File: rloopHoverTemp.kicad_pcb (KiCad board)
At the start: 2 copper layers, 30.5 x 39.4 mm, 28 parts, among them P1 CONN_01X02, P2 CONN_01X02, P3 CONN_01X01, P4 CONN_01X01, Q1 Q_NPN_BEC, Q2 Q_NPN_BEC, U1 XTR117, U2 TS305-10C50, U3 LTC2054, U4 XTR117, U5 LTC2054

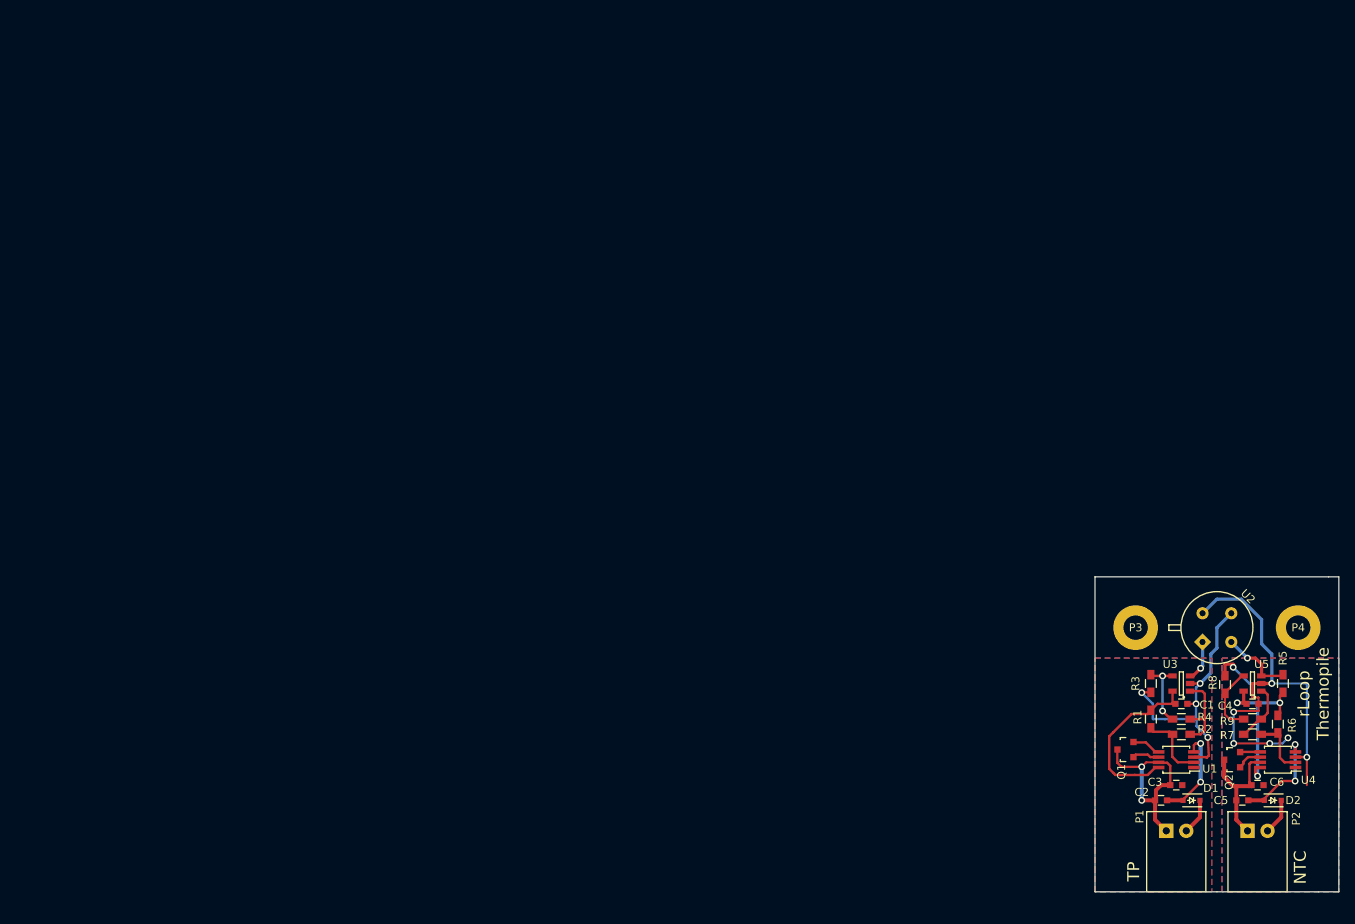
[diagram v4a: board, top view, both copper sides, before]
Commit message: complete redo with MLX sensor
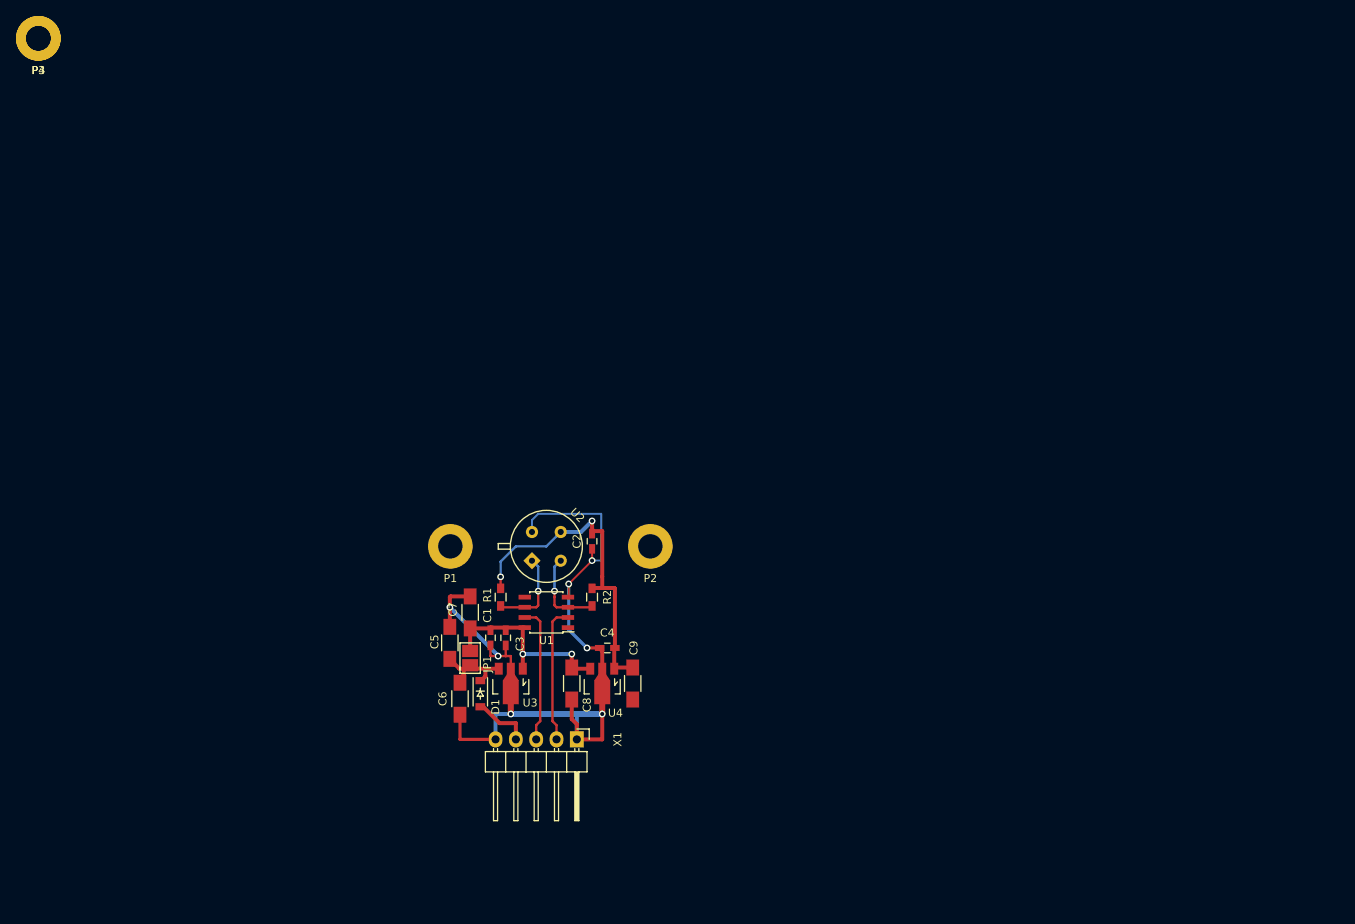
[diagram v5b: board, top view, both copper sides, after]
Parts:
- removed D2: D_Small, -footprints:SOD-323
- removed Q1, Q2: Q_NPN_BEC, TO_SOT_Packages_SMD:SOT-23
- removed R3: 825, Resistors_SMD:R_0603_HandSoldering
- removed R4: 470K, Resistors_SMD:R_0603_HandSoldering
- removed R5, R8: 100K, Resistors_SMD:R_0603_HandSoldering
- removed R6: 125K, Resistors_SMD:R_0603_HandSoldering
- removed R7: 25K, Resistors_SMD:R_0603_HandSoldering
- removed R9: 10K, Resistors_SMD:R_0603_HandSoldering
- removed U5: LTC2054, TO_SOT_Packages_SMD:SOT-23-5
- added C7: 4u7, Capacitors_SMD:C_1206_HandSoldering, F.Cu at (54.0, 71.8)
- added C8: 4u7, Capacitors_SMD:C_1206_HandSoldering, F.Cu at (66.7, 80.6)
- added C9: 4u7, Capacitors_SMD:C_1206_HandSoldering, F.Cu at (74.3, 80.6)
- added JP1: Jumper_NC_Small, -footprints:SOLDERJUMPER, F.Cu at (54.0, 77.5)
- added X1: CONN_01X05, Pin_Headers:Pin_Header_Angled_1x05, F.Cu at (67.3, 87.6)
- C1: value 100n -> C; footprint Capacitors_SMD:C_0603 -> Capacitors_SMD:C_0603_HandSoldering
- C2, C4: footprint Capacitors_SMD:C_0603 -> Capacitors_SMD:C_0603_HandSoldering
- C3: value 10n -> C; footprint Capacitors_SMD:C_0603 -> Capacitors_SMD:C_0603_HandSoldering
- C5: value 100n -> 4u7; footprint Capacitors_SMD:C_0603 -> Capacitors_SMD:C_1206_HandSoldering
- C6: value 10n -> 4u7; footprint Capacitors_SMD:C_0603 -> Capacitors_SMD:C_1206_HandSoldering
- D1: value D_Small -> D; footprint -footprints:SOD-323 -> Diodes_SMD:SOD-123
- P1, P2: value CONN_01X02 -> CONN_01X01; footprint -footprints:CONN-JST-XH-2-PTH-RGT -> -footprints:SCREWPAD-4-40
- R1: value 125K -> 4K7
- R2: value 25K -> 4K7
- U1: value XTR117 -> P82B715TD; footprint Housings_SSOP:MSOP-8_3x3mm_Pitch0.65mm -> Housings_SOIC:SOIC-8_3.9x4.9mm_Pitch1.27mm
- U2: value TS305-10C50 -> MLX90614; footprint -footprints:TS305-10C50 -> -footprints:TO39
- U3: value LTC2054 -> Regulator; footprint TO_SOT_Packages_SMD:SOT-23-5 -> -footprints:SOT89-3-VREG
- U4: value XTR117 -> Regulator; footprint Housings_SSOP:MSOP-8_3x3mm_Pitch0.65mm -> -footprints:SOT89-3-VREG
- moved P4 173.9 mm to (0.00, 0.00)
- moved P3 155.7 mm to (0.00, 0.00)
- moved C5 102.5 mm to (51.4, 75.6), turned to 90 degrees
- moved C6 98.6 mm to (52.7, 82.5), turned to 270 degrees
- moved P1 97.5 mm to (51.5, 63.5), turned to 0 degrees
- moved D1 89.9 mm to (55.2, 81.9), turned to 270 degrees
- moved C3 86.2 mm to (56.5, 74.9), turned to 270 degrees
- moved U4 85.0 mm to (70.5, 80.6)
- moved C1 84.9 mm to (58.4, 74.9), turned to 90 degrees
- moved U2 84.4 mm to (63.5, 63.5)
- moved U3 83.8 mm to (59.1, 80.6)
- moved P2 83.8 mm to (76.5, 63.5), turned to 0 degrees
- moved R1 82.7 mm to (57.8, 69.8)
- moved C4 80.9 mm to (71.1, 76.2), turned to 0 degrees
- moved U1 80.9 mm to (63.5, 71.8)
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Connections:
- C1 pad 1: /GNDA -> GND
- C1 pad 2: Net-(C1-Pad2) -> +12V
- C2 pad 1: /GNDA -> GND
- C2 pad 2: /24V_A -> +5V
- C3 pad 1: /24V_A -> +12V
- C3 pad 2: Net-(C3-Pad2) -> GND
- C4 pad 1: /GNDB -> GND
- C4 pad 2: Net-(C4-Pad2) -> +5V
- C5 pad 1: /GNDB -> Net-(C5-Pad1)
- C5 pad 2: /24V_B -> GND
- C6 pad 1: /24V_B -> Net-(C5-Pad1)
- C6 pad 2: Net-(C6-Pad2) -> GND
- D1 pad 1: Net-(D1-Pad1) -> Net-(C5-Pad1)
- D1 pad 2: Net-(C3-Pad2) -> +24V
- P1 pad 1: /24V_A -> Net-(P1-Pad1)
- P2 pad 1: /24V_B -> Net-(P2-Pad1)
- R1 pad 1: Net-(C1-Pad2) -> +5V
- R2 pad 1: Net-(R1-Pad2) -> +5V
- U1 pad 2: Net-(R1-Pad2) -> SDA
- U1 pad 3: /GNDA -> Net-(R2-Pad2)
- U1 pad 4: Net-(C3-Pad2) -> GND
- U1 pad 6: Net-(Q1-Pad1) -> Net-(R1-Pad2)
- U1 pad 7: /24V_A -> SCL
- U1 pad 8: Net-(C1-Pad2) -> +12V
- U2 pad 1: Net-(U2-Pad1) -> Net-(R1-Pad2)
- U2 pad 2: Net-(R5-Pad2) -> Net-(R2-Pad2)
- U2 pad 3: /GNDA -> +5V
- U2 pad 4: /GNDB -> GND
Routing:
- net GND: track 0.00 -> 104.3 mm, vias 0 -> 7
- net /GNDB: track 65.7 -> 0.00 mm, vias 7 -> 0
- net +5V: track 0.00 -> 42.8 mm, vias 0 -> 2
- net /GNDA: track 35.1 -> 0.00 mm, vias 4 -> 0
- net +12V: track 0.00 -> 26.2 mm, vias 0 -> 2
- net /24V_A: track 25.1 -> 0.00 mm, vias 2 -> 0
- net Net-(C1-Pad2): track 22.8 -> 0.00 mm
- net Net-(C4-Pad2): track 22.7 -> 0.00 mm, vias 3 -> 0
- net SCL: track 0.00 -> 17.1 mm
- net SDA: track 0.00 -> 17.1 mm
- net /24V_B: track 16.9 -> 0.00 mm
- net Net-(C6-Pad2): track 12.5 -> 0.00 mm, vias 2 -> 0
- net Net-(C3-Pad2): track 12.1 -> 0.00 mm, vias 2 -> 0
- net Net-(C5-Pad1): track 0.00 -> 11.7 mm
- net Net-(R5-Pad2): track 9.37 -> 0.00 mm, vias 1 -> 0
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- removed copper zone on B.Cu, net /GNDA
- removed copper zone on F.Cu, net /GNDA
- removed copper zone on B.Cu, net /GNDB
- removed copper zone on F.Cu, net /GNDB
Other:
- board outline removed
- net class 24V removed
- net class Default: clearance 0.254 -> 0.25; trace_width 0.254 -> 0.25
- rule trace_clearance: 0.254 -> 0.25
- board text removed: "NTC"
- board text removed: "TP"
- board text removed: "rLoop Thermopile"

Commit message: dual MNL connector version
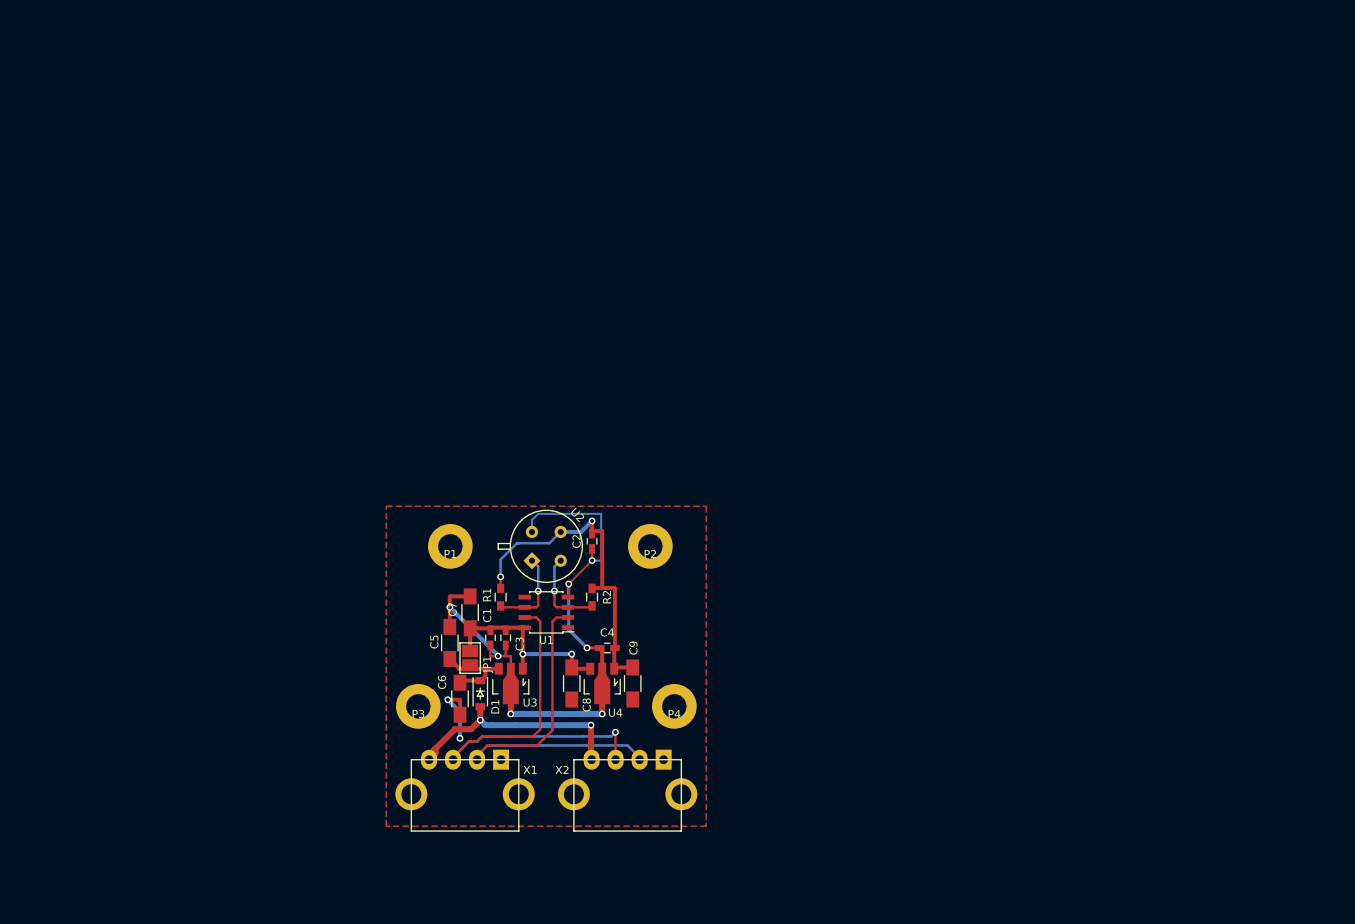
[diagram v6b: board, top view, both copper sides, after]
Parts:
- added X2: CONN_01X04-2XMNT, -footprints:CONN-TE-MICROMNL-4-PTH-MALE-RGT, F.Cu at (73.7, 90.2)
- X1: value CONN_01X05 -> CONN_01X04-2XMNT; footprint Pin_Headers:Pin_Header_Angled_1x05 -> -footprints:CONN-TE-MICROMNL-4-PTH-MALE-RGT
- moved P4 115.3 mm to (79.5, 83.5)
- moved P3 96.1 mm to (47.5, 83.5)
- moved X1 14.2 mm to (53.3, 90.2), turned to 0 degrees
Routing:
- net SCL: track 17.1 -> 53.2 mm, vias 0 -> 1
- net SDA: track 17.1 -> 49.2 mm
- net +24V: track 7.33 -> 31.6 mm, vias 0 -> 2
- net GND: track 104.3 -> 85.9 mm, vias 7 -> 9
- net Net-(C5-Pad1): track 11.7 -> 13.2 mm
- added copper zone on B.Cu, net GND
- added copper zone on F.Cu, net GND

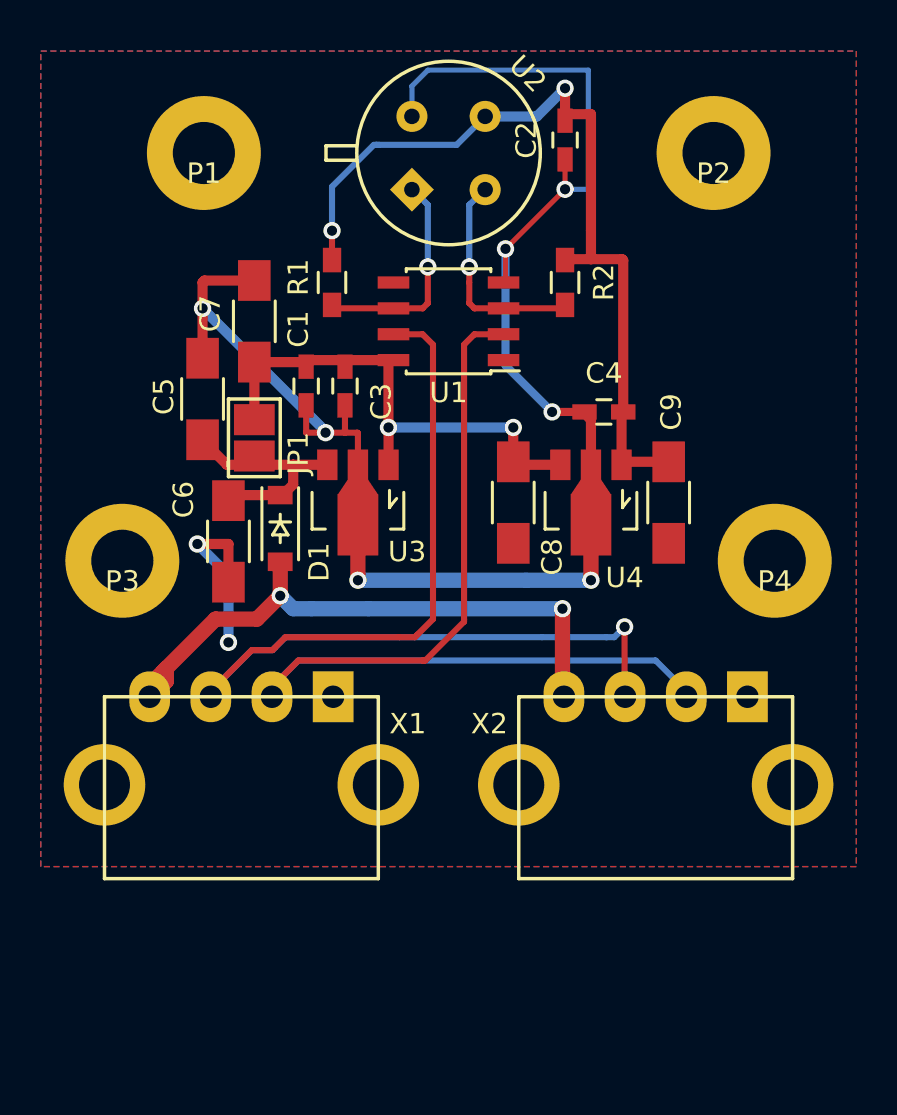
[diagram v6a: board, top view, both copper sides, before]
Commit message: version with dual RJ45 connector
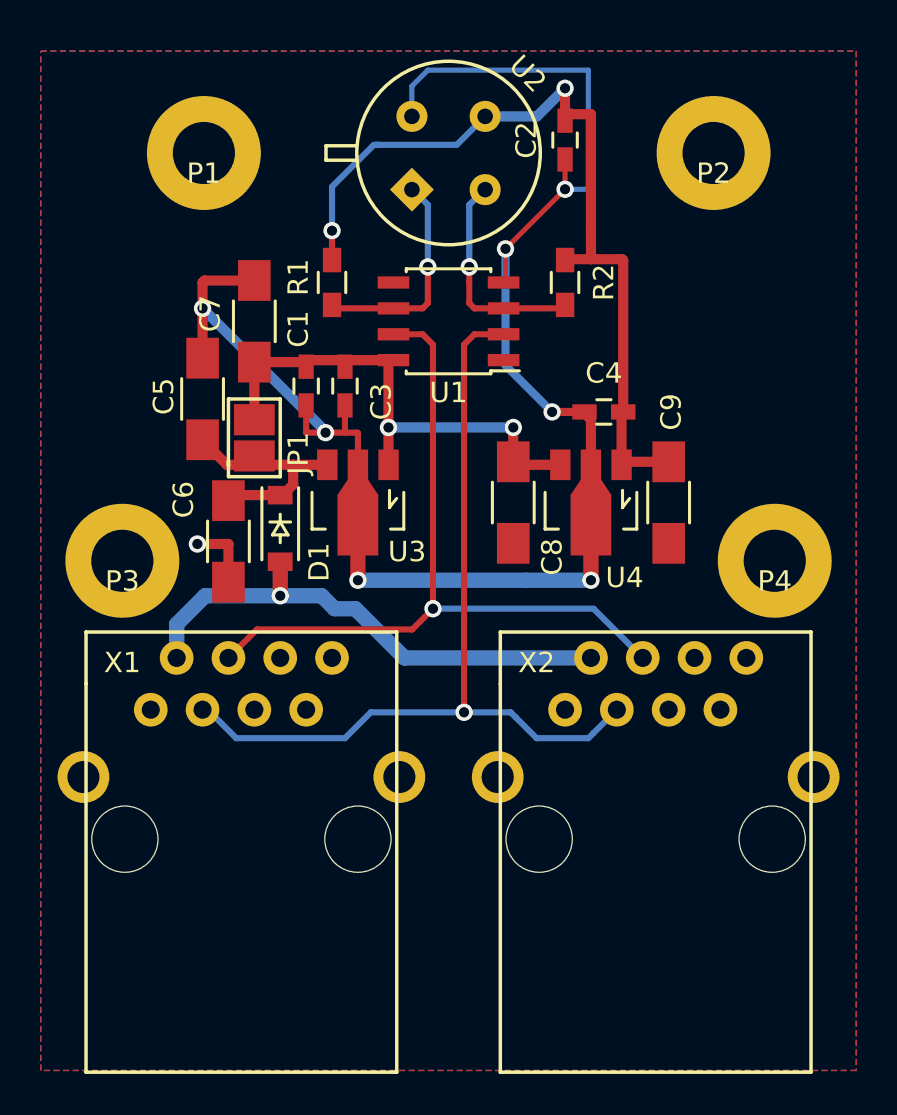
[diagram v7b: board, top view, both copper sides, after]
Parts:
- X1, X2: value CONN_01X04-2XMNT -> RJ45-SHIELDED; footprint -footprints:CONN-TE-MICROMNL-4-PTH-MALE-RGT -> -footprints:RJ45-TE-5558342-1
- moved X1 0.64 mm to (53.3, 89.5)
- moved X2 0.64 mm to (73.7, 89.5)
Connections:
- P1 pad 1: Net-(P1-Pad1) -> GND
- P2 pad 1: Net-(P2-Pad1) -> GND
- P3 pad 1: Net-(P3-Pad1) -> GND
- P4 pad 1: Net-(P4-Pad1) -> GND
- X1 pad 1: GND -> +24V
- X1 pad 2: SDA -> GND
- X1 pad 3: SCL -> SDA
- X1 pad 4: +24V -> GND
- X2 pad 1: GND -> +24V
- X2 pad 2: SDA -> GND
- X2 pad 3: SCL -> SDA
- X2 pad 4: +24V -> GND
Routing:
- net SCL: track 53.2 -> 37.4 mm
- net SDA: track 49.2 -> 42.7 mm, vias 0 -> 1
- net +24V: track 31.6 -> 25.6 mm, vias 2 -> 1
- net GND: track 85.9 -> 80.5 mm, vias 9 -> 8

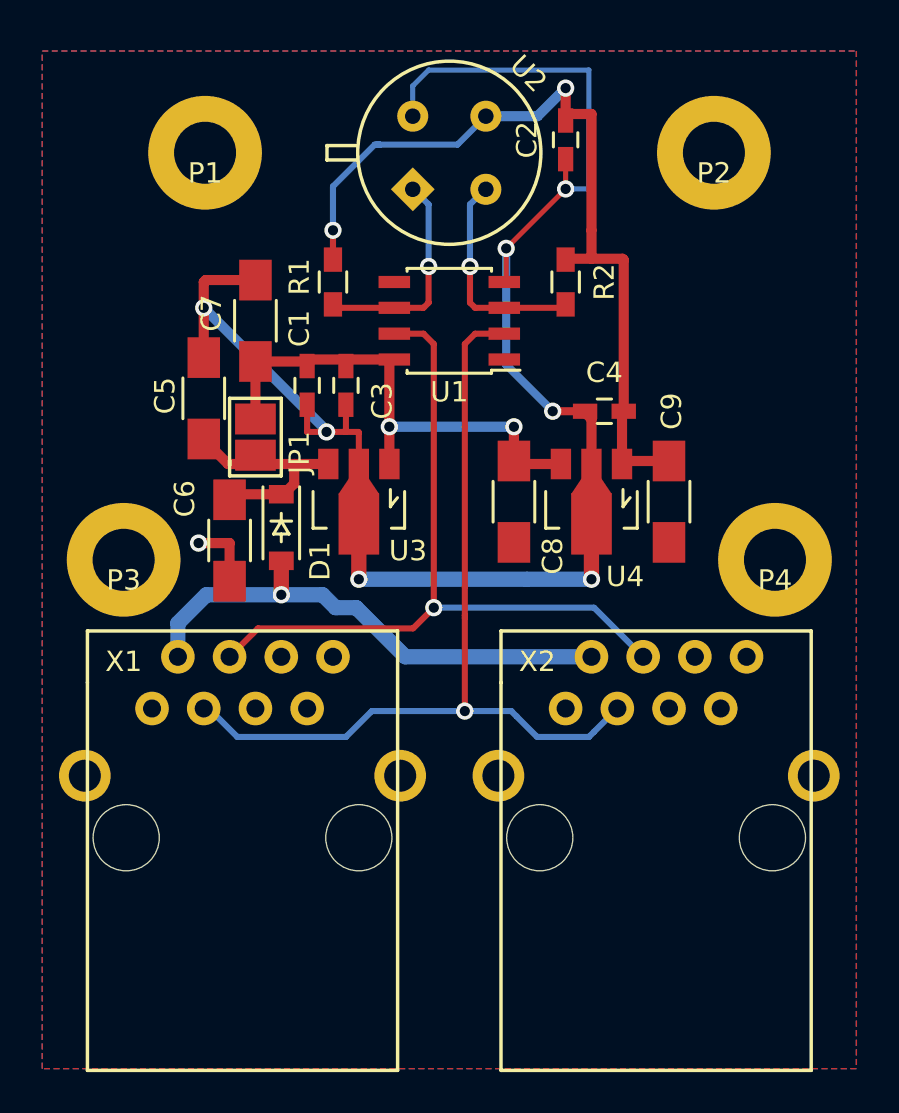
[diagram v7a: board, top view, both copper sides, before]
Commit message: different shielding scheme for RJ45
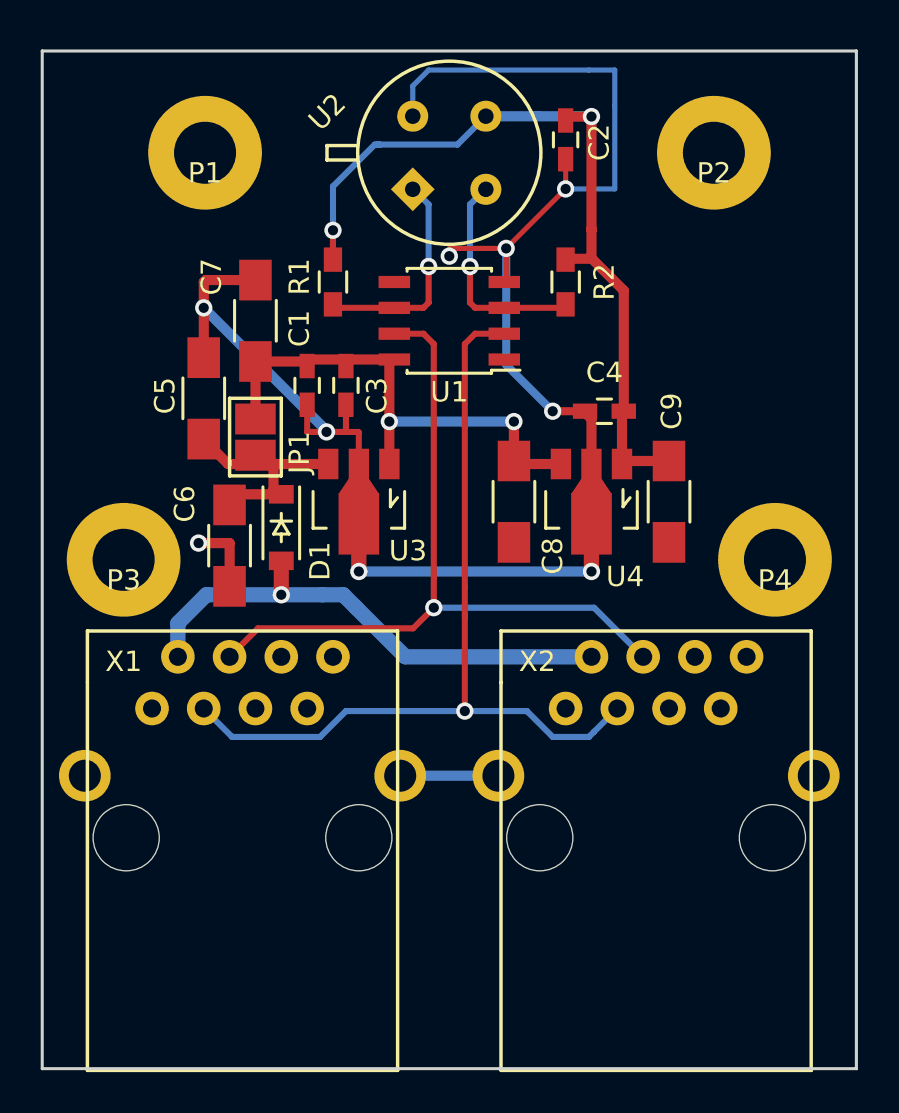
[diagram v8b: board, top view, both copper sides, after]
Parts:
- moved C6 0.25 mm to (52.7, 82.8)
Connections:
- X1 pad SHLD: GND -> /CABLE-SHIELD
- X2 pad SHLD: GND -> /CABLE-SHIELD
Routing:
- net GND: track 80.5 -> 85.4 mm, vias 8 -> 9
- net /CABLE-SHIELD: track 0.00 -> 4.83 mm
- net +5V: track 43.1 -> 41.9 mm
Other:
- board outline added: 40 x 50 mm
